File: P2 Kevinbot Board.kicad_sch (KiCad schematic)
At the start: 10 parts, among them J1 Conn_01x03_Pin, J12 Conn_02x06_Odd_Even, J16 Conn_02x06_Odd_Even, J2 Conn_01x03_Pin, J6 Conn_02x06_Odd_Even, J8 Conn_02x06_Odd_Even, U1 P2_EDGE_MODULE_SOCKET

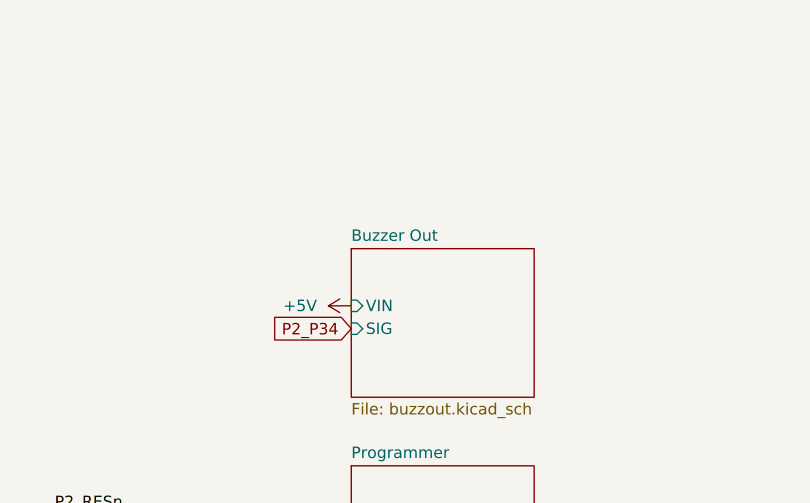
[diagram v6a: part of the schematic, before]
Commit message: Add leds, docs cleanup
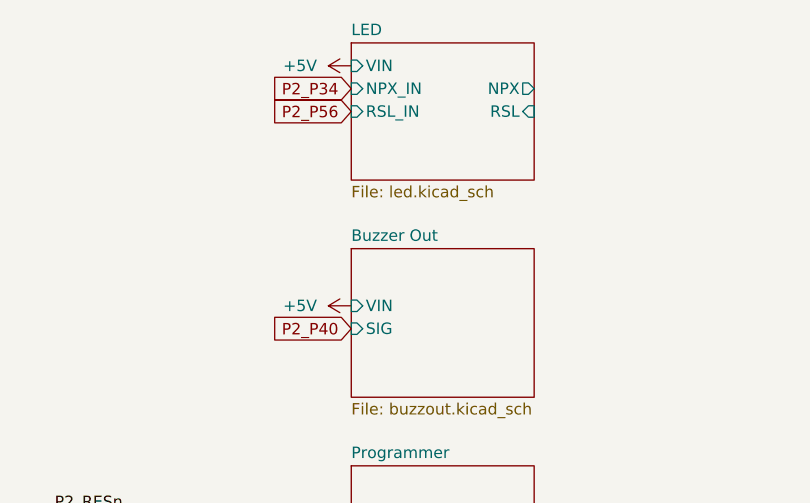
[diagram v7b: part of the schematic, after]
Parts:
- J1, J2: footprint Connector_PinHeader_2.54mm:PinHeader_1x03_P2.54mm_Vertical -> Connector_PinHeader_2.00mm:PinHeader_1x03_P2.00mm_Vertical
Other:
- added sheet LED (led.kicad_sch)
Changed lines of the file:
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@@
 		)
 	)
+	(global_label "P2_P56"
+		(shape input)
+		(at 163.83 44.45 180)
+		(fields_autoplaced yes)
+		(effects
+			(font
+				(size 1.27 1.27)
+			)
+			(justify right)
+		)
+		(property "Intersheetrefs" "${INTERSHEET_REFS}"
+			(at 153.7087 44.45 0)
+			(effects
+				(font
+					(size 1.27 1.27)
+				)
+				(justify right)
+				(hide yes)
+			)
+		)
+	)
 	(global_label "P2_P11"
 		(shape input)
@@
 		)
 	)
+	(global_label "P2_P34"
+		(shape input)
+		(at 163.83 41.91 180)
+		(fields_autoplaced yes)
+		(effects
+			(font
+				(size 1.27 1.27)
+			)
+			(justify right)
+		)
+		(property "Intersheetrefs" "${INTERSHEET_REFS}"
+			(at 153.7087 41.91 0)
+			(effects
+				(font
+					(size 1.27 1.27)
+				)
+				(justify right)
+				(hide yes)
+			)
+		)
+	)
 	(global_label "P2_P12"
 		(shape input)
@@
 		)
 	)
-	(global_label "P2_P18"
+	(global_label "P2_P40"
 		(shape input)
-		(at 90.17 114.3 0)
+		(at 163.83 68.58 180)
 		(fields_autoplaced yes)
 		(effects
@@
 				(size 1.27 1.27)
 			)
-			(justify left)
+			(justify right)
 		)
 		(property "Intersheetrefs" "${INTERSHEET_REFS}"
-			(at 99.7193 114.3794 0)
+			(at 154.2807 68.5006 0)
 			(effects
 				(font
 					(size 1.27 1.27)
 				)
-				(justify left)
+				(justify right)
 				(hide yes)
 			)
 		)
 	)
-	(global_label "P2_P46"
+	(global_label "P2_P18"
 		(shape input)
-		(at 49.53 86.36 180)
+		(at 90.17 114.3 0)
 		(fields_autoplaced yes)
 		(effects
@@
 				(size 1.27 1.27)
 			)
-			(justify right)
+			(justify left)
 		)
 		(property "Intersheetrefs" "${INTERSHEET_REFS}"
-			(at 39.4087 86.36 0)
+			(at 99.7193 114.3794 0)
 			(effects
 				(font
 					(size 1.27 1.27)
 				)
-				(justify right)
+				(justify left)
 				(hide yes)
 			)
 		)
 	)
-	(global_label "P2_P34"
+	(global_label "P2_P46"
 		(shape input)
-		(at 163.83 68.58 180)
+		(at 49.53 86.36 180)
 		(fields_autoplaced yes)
 		(effects
@@
 		)
 		(property "Intersheetrefs" "${INTERSHEET_REFS}"
-			(at 153.7087 68.58 0)
+			(at 39.4087 86.36 0)
 			(effects
 				(font
@@
 	)
 	(symbol
+		(lib_id "power:+5V")
+		(at 163.83 39.37 90)
+		(unit 1)
+		(exclude_from_sim no)
+		(in_bom yes)
+		(on_board yes)
+		(dnp no)
+		(fields_autoplaced yes)
+		(property "Reference" "#PWR037"
+			(at 167.64 39.37 0)
+			(effects
+				(font
+					(size 1.27 1.27)
+				)
+				(hide yes)
+			)
+		)
+		(property "Value" "+5V"
+			(at 160.02 39.3699 90)
+			(effects
+				(font
+					(size 1.27 1.27)
+				)
+				(justify left)
+			)
+		)
+		(property "Footprint" ""
+			(at 163.83 39.37 0)
+			(effects
+				(font
+					(size 1.27 1.27)
+				)
+				(hide yes)
+			)
+		)
+		(property "Datasheet" ""
+			(at 163.83 39.37 0)
+			(effects
+				(font
+					(size 1.27 1.27)
+				)
+				(hide yes)
+			)
+		)
+		(property "Description" "Power symbol creates a global label with name \"+5V\""
+			(at 163.83 39.37 0)
+			(effects
+				(font
+					(size 1.27 1.27)
+				)
+				(hide yes)
+			)
+		)
+		(pin "1"
+		)
+		(instances
+			(project "P2 Kevinbot Board"
+				(path "/362ca48c-0b77-4943-b8b3-fc15ab97f30d"
+					(reference "#PWR037")
+					(unit 1)
+				)
+			)
+		)
+	)
+	(symbol
 		(lib_id "Jumper:Jumper_2_Small_Bridged")
 		(at 147.32 88.9 0)
@@
 			)
 		)
-		(property "Footprint" "Connector_PinHeader_2.54mm:PinHeader_1x03_P2.54mm_Vertical"
+		(property "Footprint" "Connector_PinHeader_2.00mm:PinHeader_1x03_P2.00mm_Vertical"
 			(at 246.38 163.83 0)
 			(effects
@@
 			)
 		)
-		(property "Footprint" "Connector_PinHeader_2.54mm:PinHeader_1x03_P2.54mm_Vertical"
+		(property "Footprint" "Connector_PinHeader_2.00mm:PinHeader_1x03_P2.00mm_Vertical"
 			(at 171.45 163.83 0)
 			(effects
@@
 				)
 			)
+		)
+	)
+	(sheet
+		(at 163.83 36.83)
+		(size 20.32 15.24)
+		(exclude_from_sim no)
+		(in_bom yes)
+		(on_board yes)
+		(dnp no)
+		(fields_autoplaced yes)
+		(stroke
+			(width 0.1524)
+			(type solid)
+		)
+		(fill
+			(color 0 0 0 0.0000)
+		)
+		(property "Sheetname" "LED"
+			(at 163.83 36.1184 0)
+			(effects
+				(font
+					(size 1.27 1.27)
+				)
+				(justify left bottom)
+			)
+		)
+		(property "Sheetfile" "led.kicad_sch"
+			(at 163.83 52.6546 0)
+			(effects
+				(font
+					(size 1.27 1.27)
+				)
+				(justify left top)
+			)
+		)
+		(pin "NPX" output
+			(at 184.15 41.91 0)
+			(effects
+				(font
+					(size 1.27 1.27)
+				)
+				(justify right)
+			)
+		)
+		(pin "NPX_IN" input
+			(at 163.83 41.91 180)
+			(effects
+				(font
+					(size 1.27 1.27)
+				)
+				(justify left)
+			)
+		)
+		(pin "RSL" input
+			(at 184.15 44.45 0)
+			(effects
+				(font
+					(size 1.27 1.27)
+				)
+				(justify right)
+			)
+		)
+		(pin "RSL_IN" input
+			(at 163.83 44.45 180)
+			(effects
+				(font
+					(size 1.27 1.27)
+				)
+				(justify left)
+			)
+		)
+		(pin "VIN" input
+			(at 163.83 39.37 180)
+			(effects
+				(font
+					(size 1.27 1.27)
+				)
+				(justify left)
+			)
+		)
+		(instances
+			(project "P2 Kevinbot Board"
+				(path "/362ca48c-0b77-4943-b8b3-fc15ab97f30d"
+					(page "4")
+				)
+			)

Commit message: reset button
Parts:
- added J9: Conn_01x02_Pin, Connector_Molex:Molex_Nano-Fit_105309-xx02_1x02_P2.50mm_Vertical, symbol Connector:Conn_01x02_Pin
- added SW1: SW_Push, Button_Switch_SMD:SW_SPST_PTS645, symbol Switch:SW_Push
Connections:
- net GND: now also J9.1 (Pin_1), SW1.2
- net P2_RESn: now also J9.2 (Pin_2), SW1.1
